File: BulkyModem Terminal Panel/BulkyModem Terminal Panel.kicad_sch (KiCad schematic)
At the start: 16 parts, among them J1 Front Panel, M1 Mounting_Pin, M2 Mounting_Pin, M3 Mounting_Pin, M4 Mounting_Pin, SW1 MODE, SW2 POW, SW3 DEFAULT, SW4 RESET

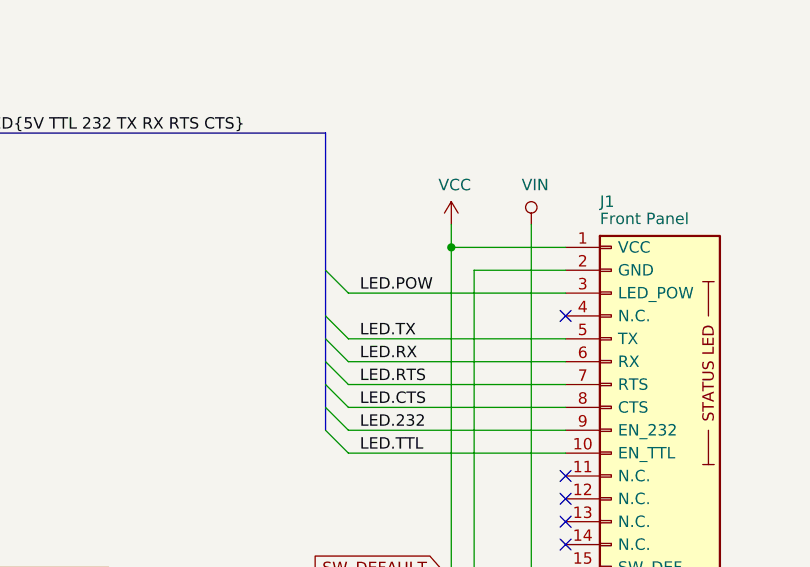
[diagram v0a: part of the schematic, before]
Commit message: Missing a trace
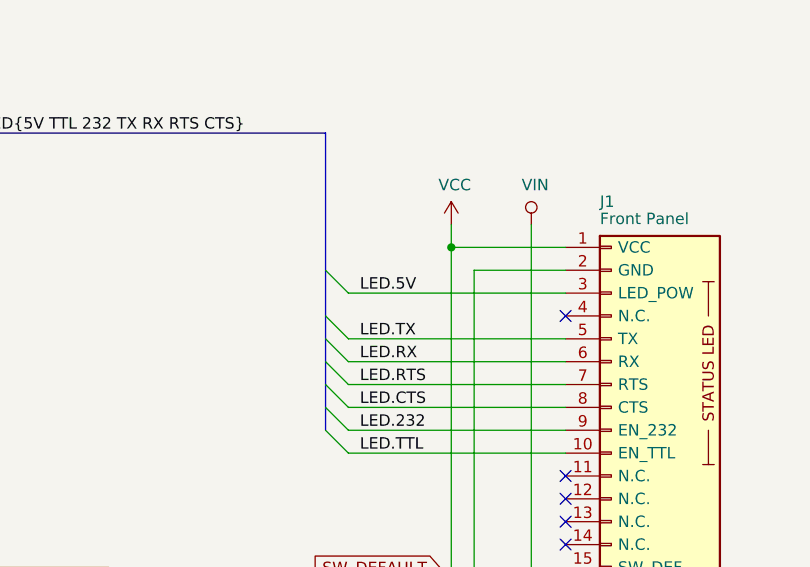
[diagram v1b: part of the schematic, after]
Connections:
- net LED.POW is gone; now on net LED.5V: J1.3 (LED_POW)
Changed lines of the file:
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@@
 		)
 	)
-	(label "LED.POW"
+	(label "LED.5V"
 		(at 210.82 78.74 0)
 		(fields_autoplaced yes)

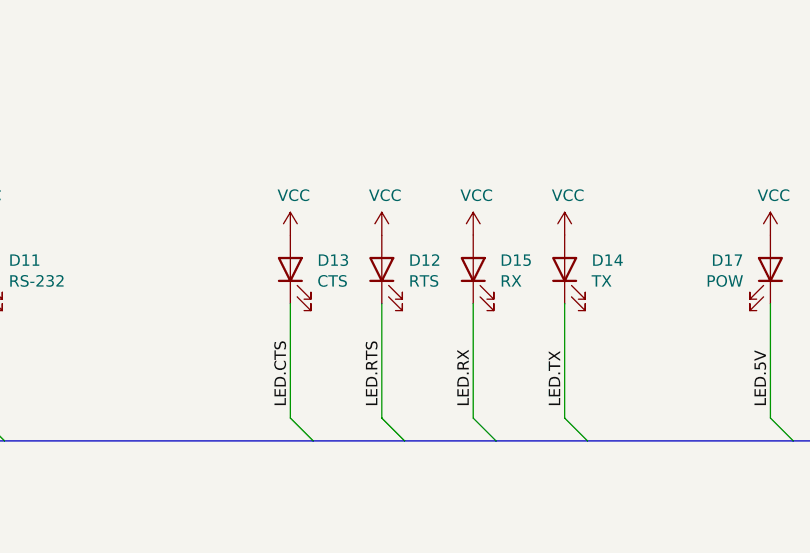
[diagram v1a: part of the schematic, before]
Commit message: Flipped serial LEDs
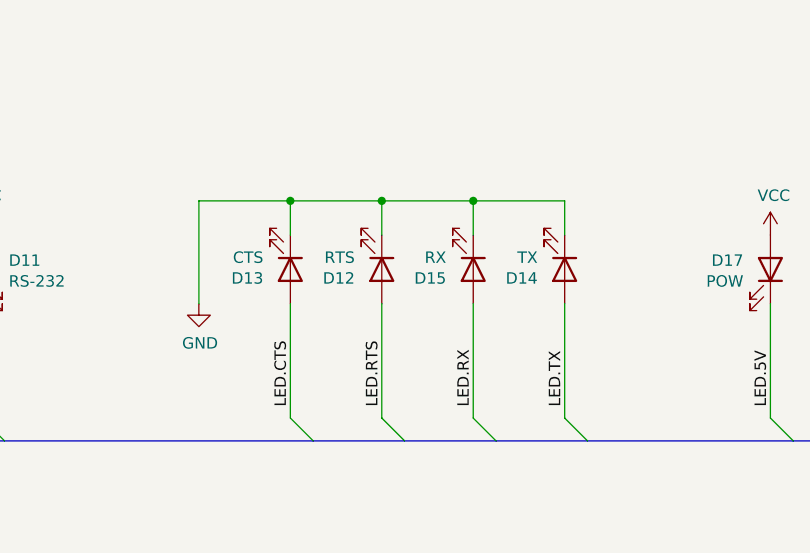
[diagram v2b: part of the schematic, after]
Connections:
- net GND: now also D12.1 (K), D13.1 (K), D14.1 (K), D15.1 (K)
- net LED.CTS: now also D13.2 (A); no longer D13.1 (K)
- net LED.RTS: now also D12.2 (A); no longer D12.1 (K)
- net LED.RX: now also D15.2 (A); no longer D15.1 (K)
- net LED.TX: now also D14.2 (A); no longer D14.1 (K)
- net VCC: no longer D12.2 (A), D13.2 (A), D14.2 (A), D15.2 (A)
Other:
- moved on the sheet: D12, D13, D14, D15
